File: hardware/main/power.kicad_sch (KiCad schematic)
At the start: 30 parts, among them Q1 SSM3J338R, Q2 BCP53, Q3 SSM3J338R, Q4 BC817, Q5 SSM3J338R, Q6 BC807, Q7 BC817, U5 AP2114H-3.3, U7 LM358

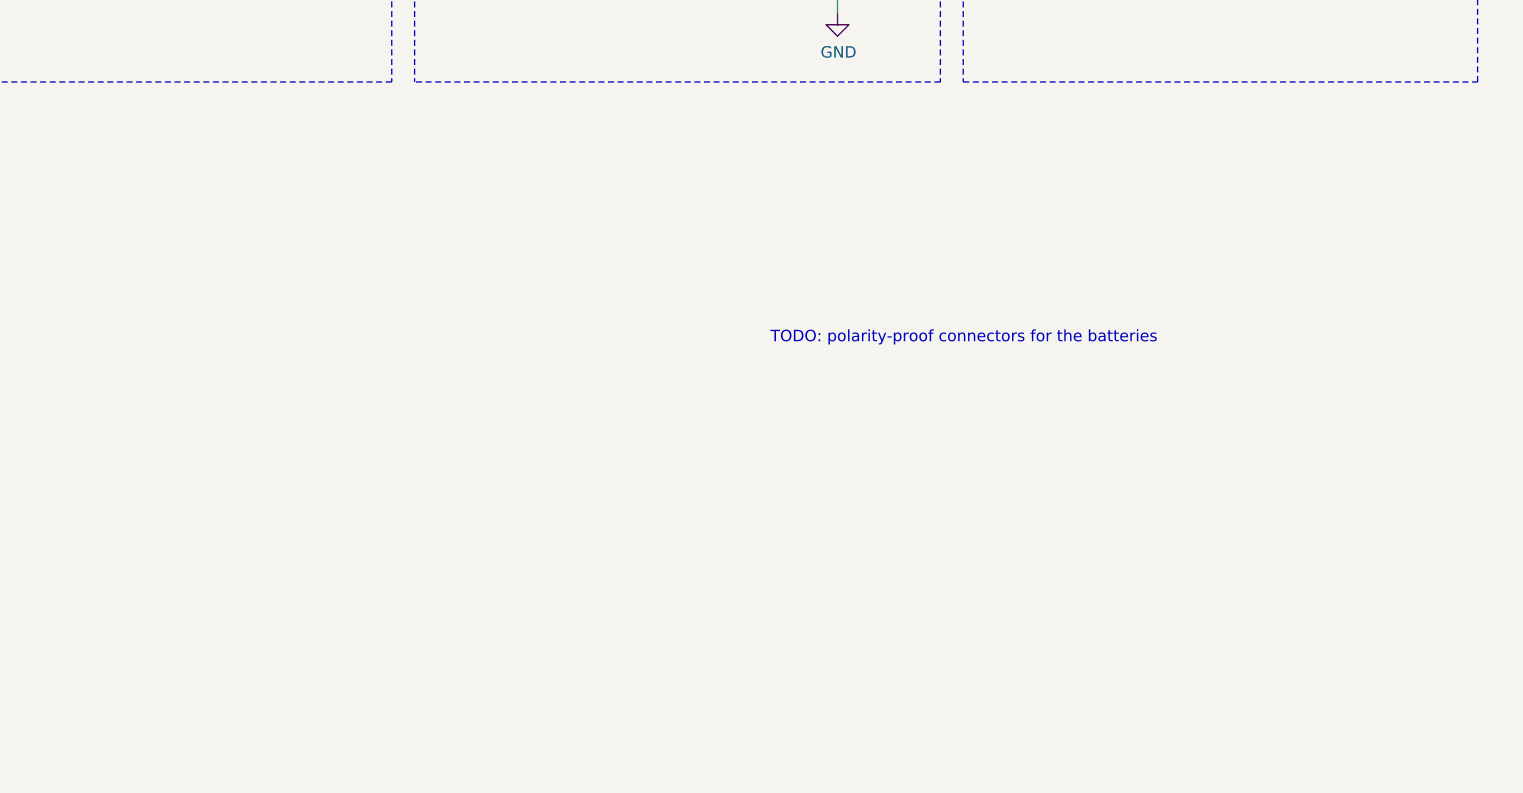
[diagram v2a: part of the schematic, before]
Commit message: Add circuit to disconnect the shift registers
This is done to save energy when the keyboard is switched off.
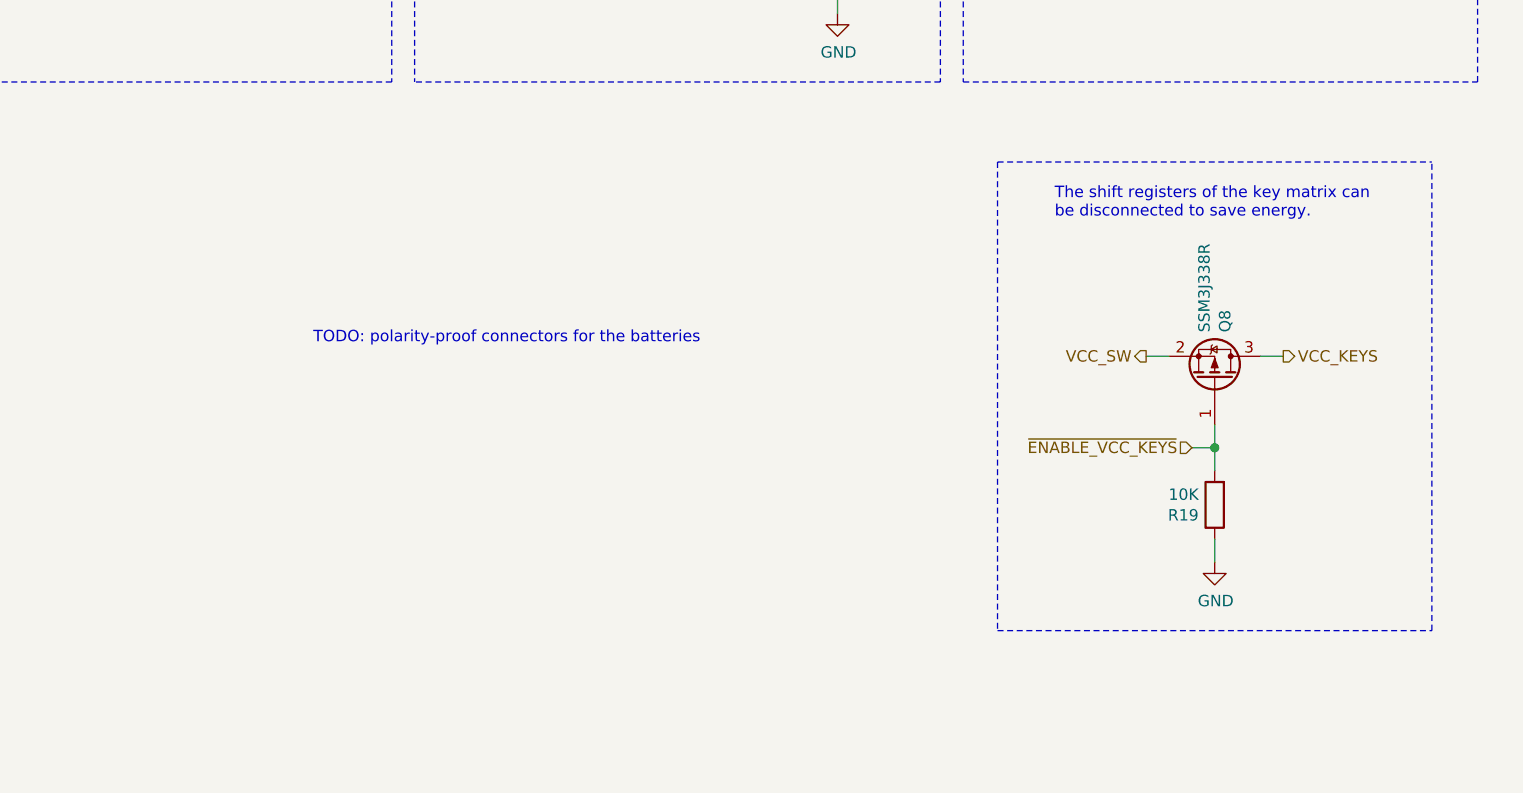
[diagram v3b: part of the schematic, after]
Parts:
- added Q8: SSM3J338R, Package_TO_SOT_SMD:SOT-23_Handsoldering, symbol Device:Q_PMOS_GSD
- added R19: 10K, Resistor_SMD:R_0603_1608Metric, symbol Device:R
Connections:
- net GND: now also R19.1
- net VCC_SW: now also Q8.2 (S)
- new net VCC_KEYS: Q8.3 (D)
- new net ~ENABLE_VCC_KEYS: Q8.1 (G), R19.2
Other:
- note added: "The shift registers of the key matrix can be disconnected to save energy."
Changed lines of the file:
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@@
   (junction (at 245.11 31.75) (diameter 1.016) (color 0 0 0 0))
   (junction (at 252.73 57.15) (diameter 1.016) (color 0 0 0 0))
+  (junction (at 252.73 140.97) (diameter 1.016) (color 0 0 0 0))
   (junction (at 267.97 46.99) (diameter 1.016) (color 0 0 0 0))
   (no_connect (at 275.59 31.75))
@@
     (stroke (width 0) (type solid) (color 0 0 0 0))
   )
+  (wire (pts (xy 245.11 130.81) (xy 247.65 130.81))
+    (stroke (width 0) (type solid) (color 0 0 0 0))
+  )
   (wire (pts (xy 247.65 46.99) (xy 242.57 46.99))
     (stroke (width 0) (type solid) (color 0 0 0 0))
   )
+  (wire (pts (xy 250.19 140.97) (xy 252.73 140.97))
+    (stroke (width 0) (type solid) (color 0 0 0 0))
+  )
   (wire (pts (xy 252.73 54.61) (xy 252.73 57.15))
     (stroke (width 0) (type solid) (color 0 0 0 0))
@@
     (stroke (width 0) (type solid) (color 0 0 0 0))
   )
+  (wire (pts (xy 252.73 138.43) (xy 252.73 140.97))
+    (stroke (width 0) (type solid) (color 0 0 0 0))
+  )
+  (wire (pts (xy 252.73 140.97) (xy 252.73 143.51))
+    (stroke (width 0) (type solid) (color 0 0 0 0))
+  )
+  (wire (pts (xy 252.73 151.13) (xy 252.73 153.67))
+    (stroke (width 0) (type solid) (color 0 0 0 0))
+  )
+  (wire (pts (xy 257.81 130.81) (xy 260.35 130.81))
+    (stroke (width 0) (type solid) (color 0 0 0 0))
+  )
   (wire (pts (xy 260.35 31.75) (xy 245.11 31.75))
     (stroke (width 0) (type solid) (color 0 0 0 0))
@@
   )
   (polyline (pts (xy 224.79 100.33) (xy 281.94 100.33))
+    (stroke (width 0) (type dash) (color 0 0 0 0))
+  )
+  (polyline (pts (xy 228.6 109.22) (xy 228.6 161.29))
+    (stroke (width 0) (type dash) (color 0 0 0 0))
+  )
+  (polyline (pts (xy 228.6 109.22) (xy 276.86 109.22))
+    (stroke (width 0) (type dash) (color 0 0 0 0))
+  )
+  (polyline (pts (xy 228.6 161.29) (xy 276.86 161.29))
+    (stroke (width 0) (type dash) (color 0 0 0 0))
+  )
+  (polyline (pts (xy 276.86 161.29) (xy 276.86 109.22))
     (stroke (width 0) (type dash) (color 0 0 0 0))
   )
@@
     (effects (font (size 1.27 1.27)) (justify left bottom))
   )
+  (text "TODO: polarity-proof connectors for the batteries" (at 195.58 129.54 180)
+    (effects (font (size 1.27 1.27)) (justify right bottom))
+  )
   (text "Supply the keyboard with 3.3V from a programmer\nif available, and disconnect the battery."
     (at 226.06 22.86 0)
     (effects (font (size 1.27 1.27)) (justify left bottom))
   )
-  (text "TODO: polarity-proof connectors for the batteries" (at 246.38 129.54 180)
-    (effects (font (size 1.27 1.27)) (justify right bottom))
+  (text "The shift registers of the key matrix can\nbe disconnected to save energy."
+    (at 234.95 115.57 0)
+    (effects (font (size 1.27 1.27)) (justify left bottom))
   )
   (hierarchical_label "CHARGE" (shape input) (at 127 69.85 90)
@@
     (effects (font (size 1.27 1.27)) (justify left))
   )
+  (hierarchical_label "VCC_SW" (shape output) (at 245.11 130.81 180)
+    (effects (font (size 1.27 1.27)) (justify right))
+  )
+  (hierarchical_label "~ENABLE_VCC_KEYS" (shape input) (at 250.19 140.97 180)
+    (effects (font (size 1.27 1.27)) (justify right))
+  )
+  (hierarchical_label "VCC_KEYS" (shape output) (at 260.35 130.81 0)
+    (effects (font (size 1.27 1.27)) (justify left))
+  )
   (hierarchical_label "VCC_SW" (shape output) (at 270.51 46.99 0)
     (effects (font (size 1.27 1.27)) (justify left))
@@
     )
     (property "Datasheet" "" (id 3) (at 252.73 69.85 0)
+      (effects (font (size 1.27 1.27)) hide)
+    )
+  )
+  (symbol (lib_id "power:GND") (at 252.73 153.67 0) (unit 1)
+    (in_bom yes) (on_board yes)
+    (property "Reference" "#PWR0122" (id 0) (at 252.73 160.02 0)
+      (effects (font (size 1.27 1.27)) hide)
+    )
+    (property "Value" "GND" (id 1) (at 252.8443 157.9944 0))
+    (property "Footprint" "" (id 2) (at 252.73 153.67 0)
+      (effects (font (size 1.27 1.27)) hide)
+    )
+    (property "Datasheet" "" (id 3) (at 252.73 153.67 0)
       (effects (font (size 1.27 1.27)) hide)
     )
@@
     )
     (property "Datasheet" "~" (id 3) (at 252.73 63.5 0)
+      (effects (font (size 1.27 1.27)) hide)
+    )
+  )
+  (symbol (lib_id "Device:R") (at 252.73 147.32 180) (unit 1)
+    (in_bom yes) (on_board yes)
+    (property "Reference" "R19" (id 0) (at 250.9519 148.4694 0)
+      (effects (font (size 1.27 1.27)) (justify left))
+    )
+    (property "Value" "10K" (id 1) (at 250.952 146.171 0)
+      (effects (font (size 1.27 1.27)) (justify left))
+    )
+    (property "Footprint" "Resistor_SMD:R_0603_1608Metric" (id 2) (at 254.508 147.32 90)
+      (effects (font (size 1.27 1.27)) hide)
+    )
+    (property "Datasheet" "~" (id 3) (at 252.73 147.32 0)
       (effects (font (size 1.27 1.27)) hide)
     )
@@
       (effects (font (size 1.27 1.27)) hide)
     )
+  )
+  (symbol (lib_id "Device:Q_PMOS_GSD") (at 252.73 133.35 270) (mirror x) (unit 1)
+    (in_bom yes) (on_board yes)
+    (property "Reference" "Q8" (id 0) (at 253.8794 128.1429 0)
+      (effects (font (size 1.27 1.27)) (justify left))
+    )
+    (property "Value" "SSM3J338R" (id 1) (at 251.581 128.143 0)
+      (effects (font (size 1.27 1.27)) (justify left))
+    )
+    (property "Footprint" "Package_TO_SOT_SMD:SOT-23_Handsoldering" (id 2) (at 255.27 128.27 0)
+      (effects (font (size 1.27 1.27)) hide)
+    )
+    (property "Datasheet" "~" (id 3) (at 252.73 133.35 0)
+      (effects (font (size 1.27 1.27)) hide)
+    )
+    (property "Part Name" "Toshiba SSM3J338R" (id 4) (at 252.73 133.35 0)
+      (effects (font (size 1.27 1.27)) hide)
+    )
+    (property "Mouser" "757-SSM3J338RLF" (id 5) (at 252.73 133.35 0)
+      (effects (font (size 1.27 1.27)) hide)
+    )
